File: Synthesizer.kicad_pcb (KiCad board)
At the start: 6 copper layers, 169 parts, among them J1 USB_A, J2 AudioJack3, J3 USB_B_Micro, J4 FPGA_debug, J5 MCU_debug, J6 67997-410HLF, SW1 SW_Push, SW10 SW_Push, SW11 SW_Push, SW12 SW_Push, SW13 SW_Push, SW14 SW_Push, SW15 SW_Push, SW16 SW_Push, SW2 SW_Push, SW3 SW_Push, SW4 SW_Push, SW5 SW_Push, SW6 SW_Push, SW7 SW_Push, SW8 SW_Push, SW9 SW_Push, U1 TPD3S014, U2 S25FL127S, U3 XC7A100T-FTG256, U4 Oscillator, U5 TPS54325, U6 TPS54294, U7 EFM32GG11B4xx, U8 PCM5102, Y1 48Mhz

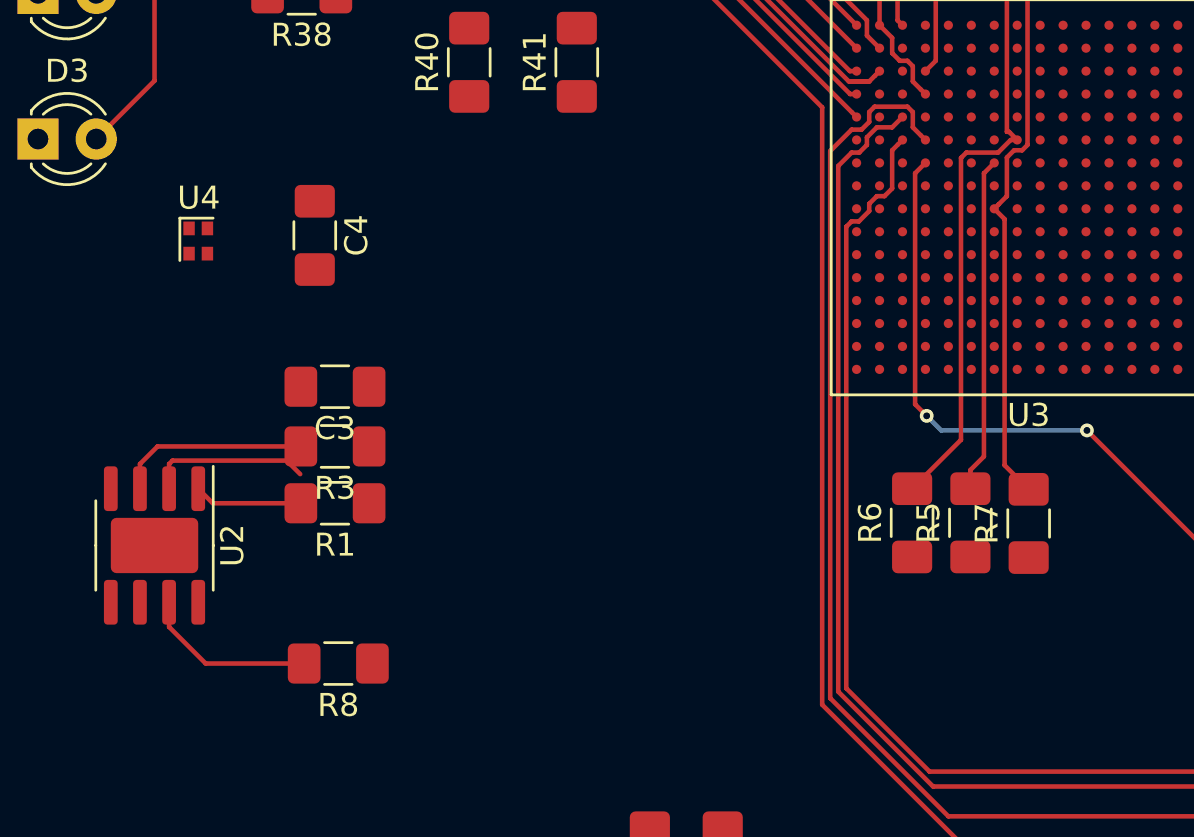
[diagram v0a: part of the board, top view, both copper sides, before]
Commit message: Started wiring the flash chip.
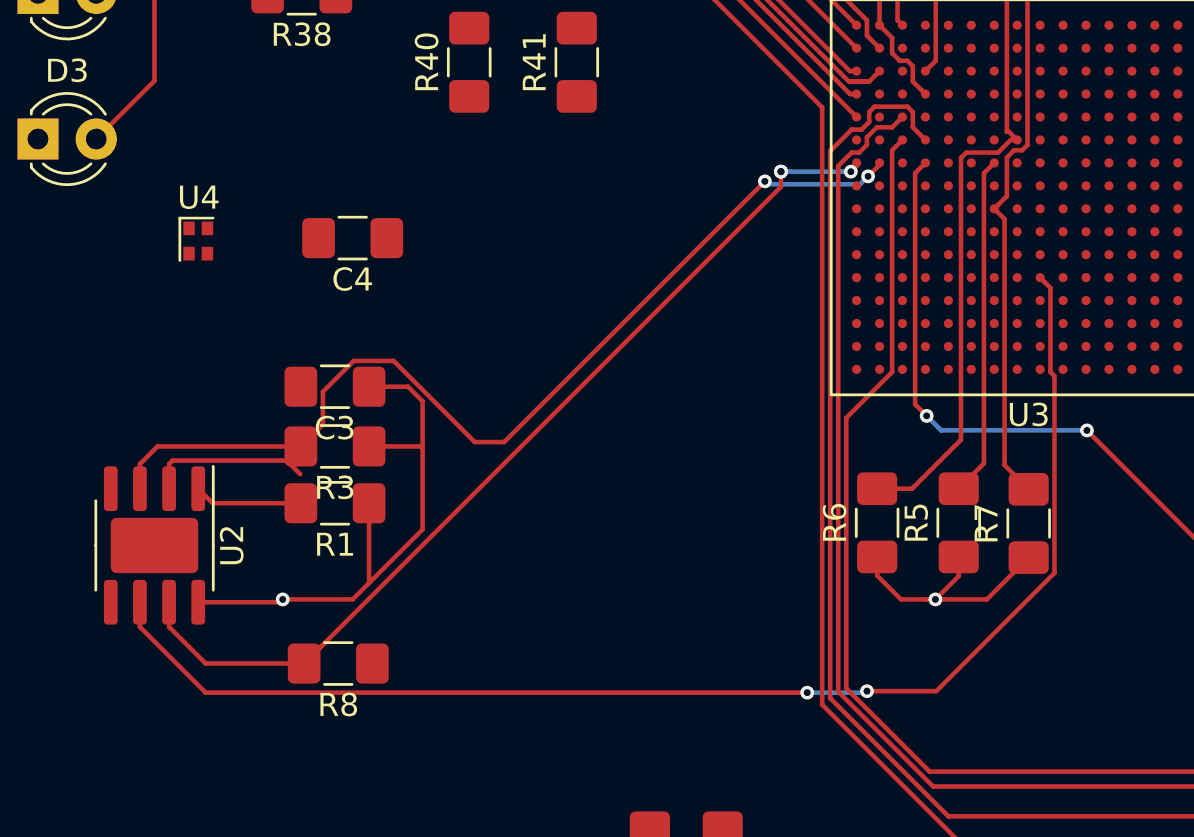
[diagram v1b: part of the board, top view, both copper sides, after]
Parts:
- moved C4 1.66 mm to (34.0, 91.9), turned to 180 degrees
- moved R6 1.52 mm to (56.9, 104.4)
- moved R5 0.51 mm to (60.5, 104.4)
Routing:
- net Net-(U2-Pad6): track 0.00 -> 57.4 mm, vias 0 -> 2
- net +3V3: track 6.42 -> 42.4 mm, vias 2 -> 4
- net Net-(R8-Pad2): track 8.09 -> 42.8 mm, vias 0 -> 3
- net Net-(R3-Pad2): track 8.87 -> 43.2 mm, vias 0 -> 2
- net /EFM32/FPGA_Reset: track 54.0 -> 55.6 mm

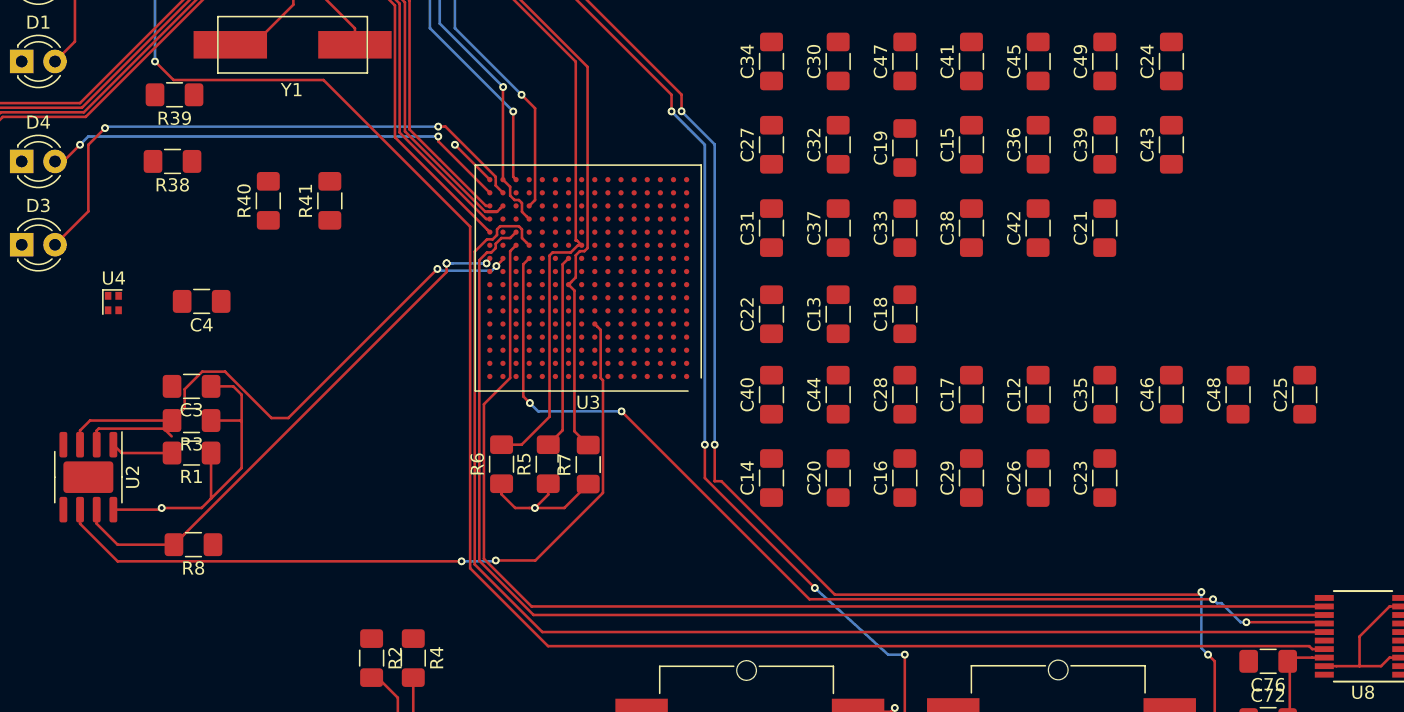
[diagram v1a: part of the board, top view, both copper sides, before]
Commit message: Fix via diameters to fit FPGA and fix some via connections
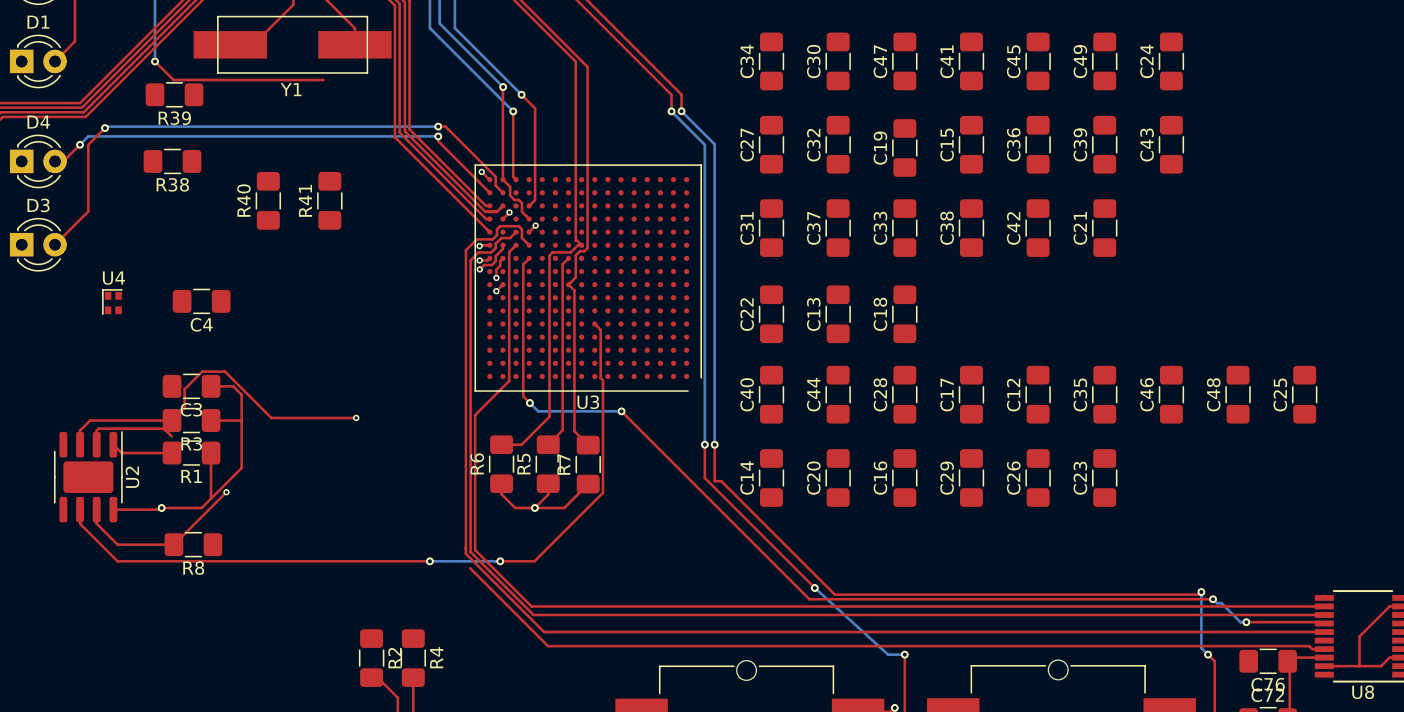
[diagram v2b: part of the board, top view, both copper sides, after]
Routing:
- net /Audio DAC/Soft-mute: track 150.1 -> 108.3 mm
- net Net-(R8-Pad2): track 42.8 -> 41.2 mm, vias 3 -> 2
- net +3V3: track 42.4 -> 43.9 mm, vias 4 -> 6
- net GND: track 43.9 -> 45.3 mm, vias 7 -> 10
- net /Artix7/DAC_LRCK: track 96.9 -> 98.0 mm
- net /Audio DAC/Bit-clock: track 92.9 -> 93.8 mm
- net /Artix7/DAC_SCK: track 90.5 -> 91.0 mm
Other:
- net class +5V internal: via_dia 0.6 -> 0.48; via_drill 0.3 -> 0.25
- net class Default: via_dia 0.6 -> 0.48; via_drill 0.3 -> 0.25
- rule via_min_drill: 0.3 -> 0.25
- rule via_min_size: 0.6 -> 0.48

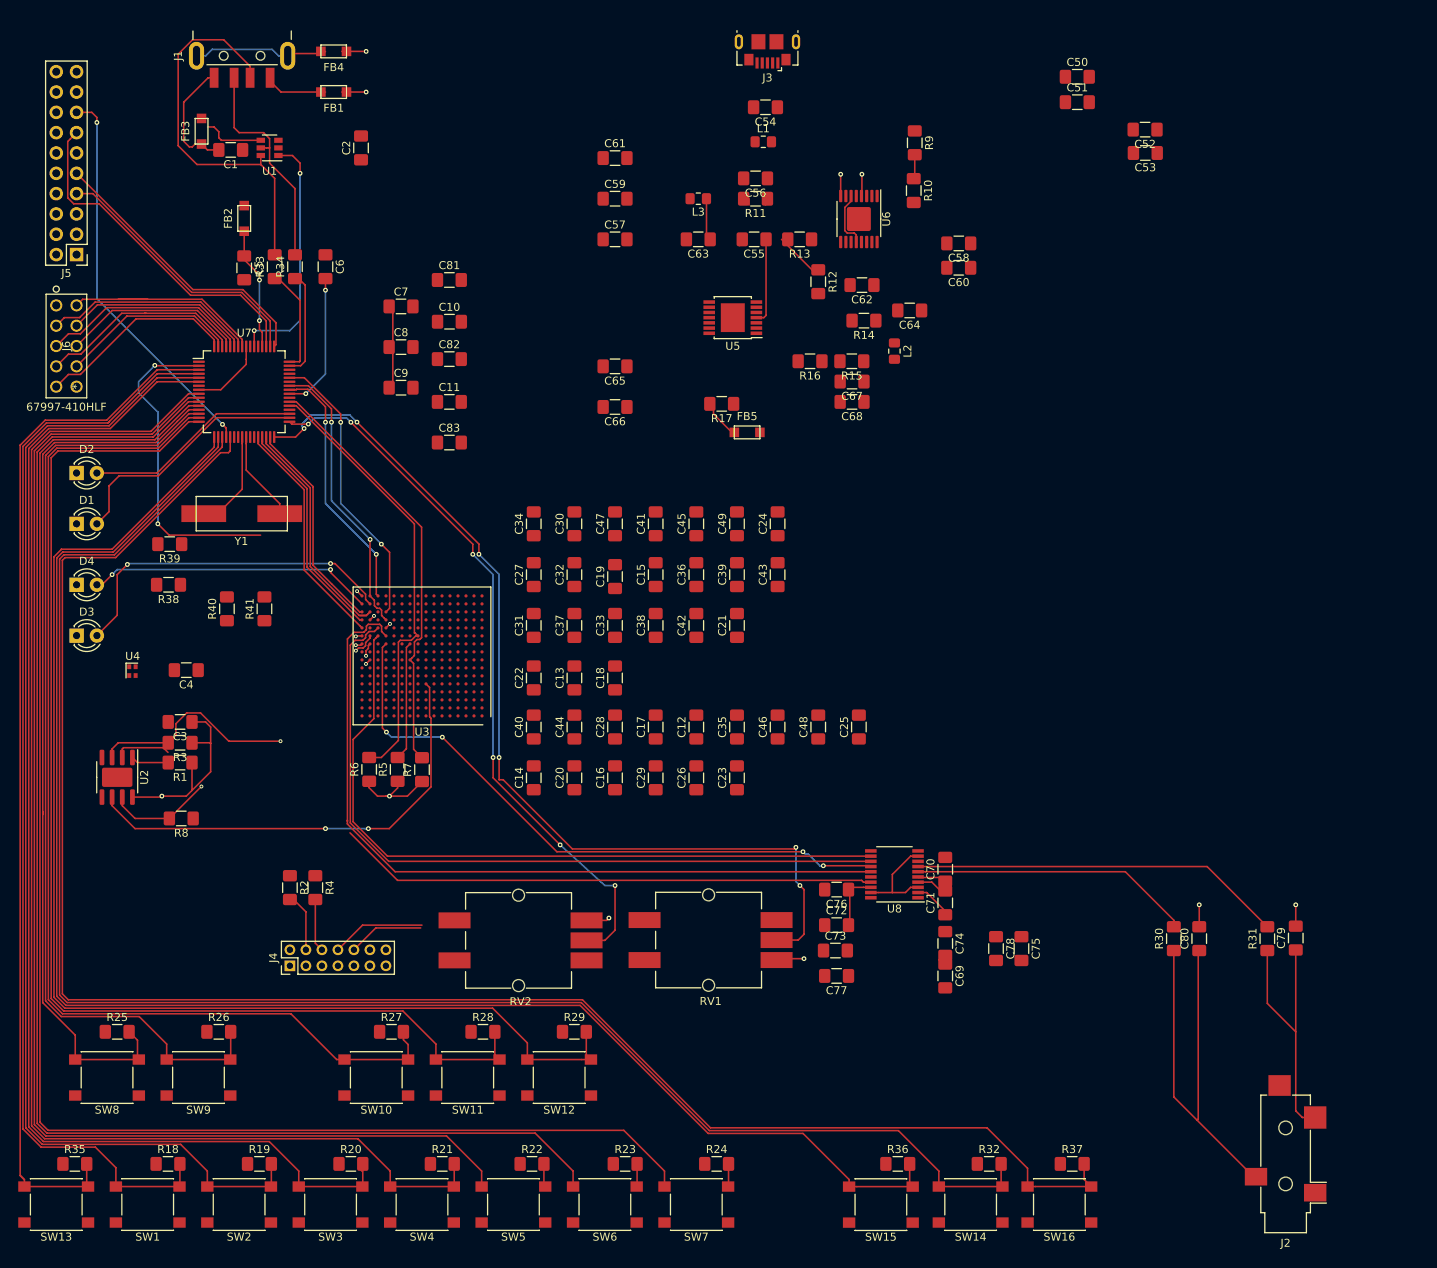
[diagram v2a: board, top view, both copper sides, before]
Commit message: Add vias to most FPGA pins and reroute many long surface traces through them
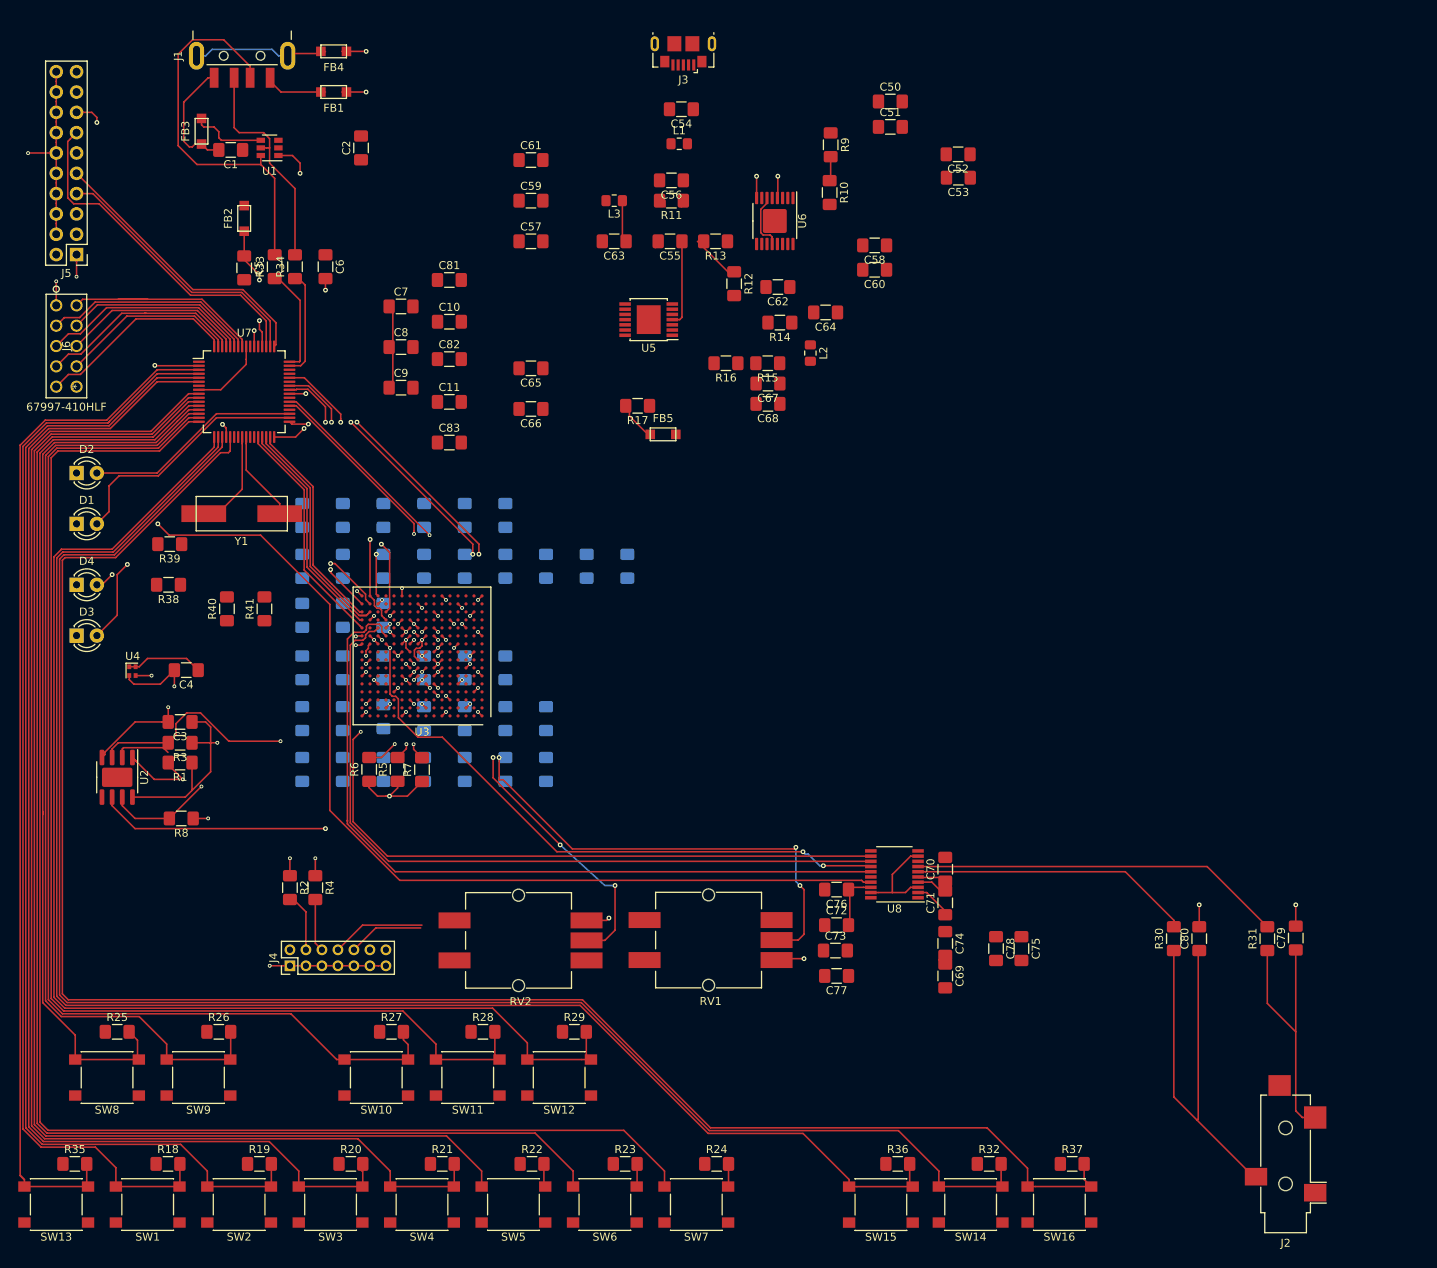
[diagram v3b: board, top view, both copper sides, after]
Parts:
- C12, C13, C14, C15, C16, C17, C18, C19, C20, C21, C22, C23, C24, C25, C26, C27, C28, C29, C30, C31, C32, C33, C34, C35, C36, C37, C38, C39, C40, C41, C42, C43, C44, C45, C46, C47, C48, C49: moved to B.Cu
- moved C23 43.7 mm to (73.9, 72.6), turned to 270 degrees
- moved C26 43.7 mm to (68.8, 72.6), turned to 270 degrees
- moved C14 43.7 mm to (48.5, 72.6), turned to 270 degrees
- moved C16 43.7 mm to (58.7, 72.6), turned to 270 degrees
- moved C20 43.7 mm to (53.6, 72.6), turned to 270 degrees
- moved C29 43.7 mm to (63.8, 72.6), turned to 270 degrees
- moved C24 42.2 mm to (79.0, 104.4), turned to 270 degrees
- moved C45 42.2 mm to (68.8, 104.4), turned to 270 degrees
- moved C49 42.2 mm to (73.9, 104.4), turned to 270 degrees
- moved C30 42.2 mm to (53.6, 104.4), turned to 270 degrees
- moved C34 42.2 mm to (48.5, 104.4), turned to 270 degrees
- moved C41 42.2 mm to (63.8, 104.4), turned to 270 degrees
- moved C47 42.2 mm to (58.7, 104.4), turned to 270 degrees
- moved C12 35.2 mm to (68.8, 79.0), turned to 270 degrees
- moved C25 35.2 mm to (89.2, 79.0), turned to 270 degrees
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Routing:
- net GND: track 45.3 -> 136.7 mm, vias 10 -> 51
- net /Audio DAC/Soft-mute: track 108.3 -> 149.9 mm
- net Net-(R1-Pad2): track 5.20 -> 46.0 mm, vias 0 -> 2
- net Net-(U3-PadN11): track 0.00 -> 36.2 mm, vias 0 -> 2
- net +3V3: track 43.9 -> 71.7 mm, vias 6 -> 17
- net +1V0: track 0.00 -> 8.98 mm, vias 0 -> 5
- net +1V8: track 0.00 -> 4.53 mm, vias 0 -> 3
- net /Audio DAC/Audio-data: track 78.9 -> 76.9 mm, vias 4 -> 3
- net Net-(FB3-Pad1): track 7.78 -> 9.45 mm
- net Net-(R5-Pad2): track 14.8 -> 16.2 mm, vias 0 -> 2
- net /EFM32/FPGA_Ready: track 53.3 -> 54.6 mm, vias 0 -> 3
- net Net-(J4-Pad6): track 7.09 -> 7.80 mm, vias 0 -> 1
- net Net-(J4-Pad4): track 7.57 -> 8.29 mm, vias 0 -> 1
- net /Artix7/DAC_SCK: track 91.0 -> 91.4 mm, vias 0 -> 2
- net /EFM32/FPGA_Reset: track 55.6 -> 55.3 mm, vias 0 -> 3
